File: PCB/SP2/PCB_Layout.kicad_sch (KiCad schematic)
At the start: 5 parts, among them J1 PA1010D, J2 SD Card, J3 BNO055, U1 Pico

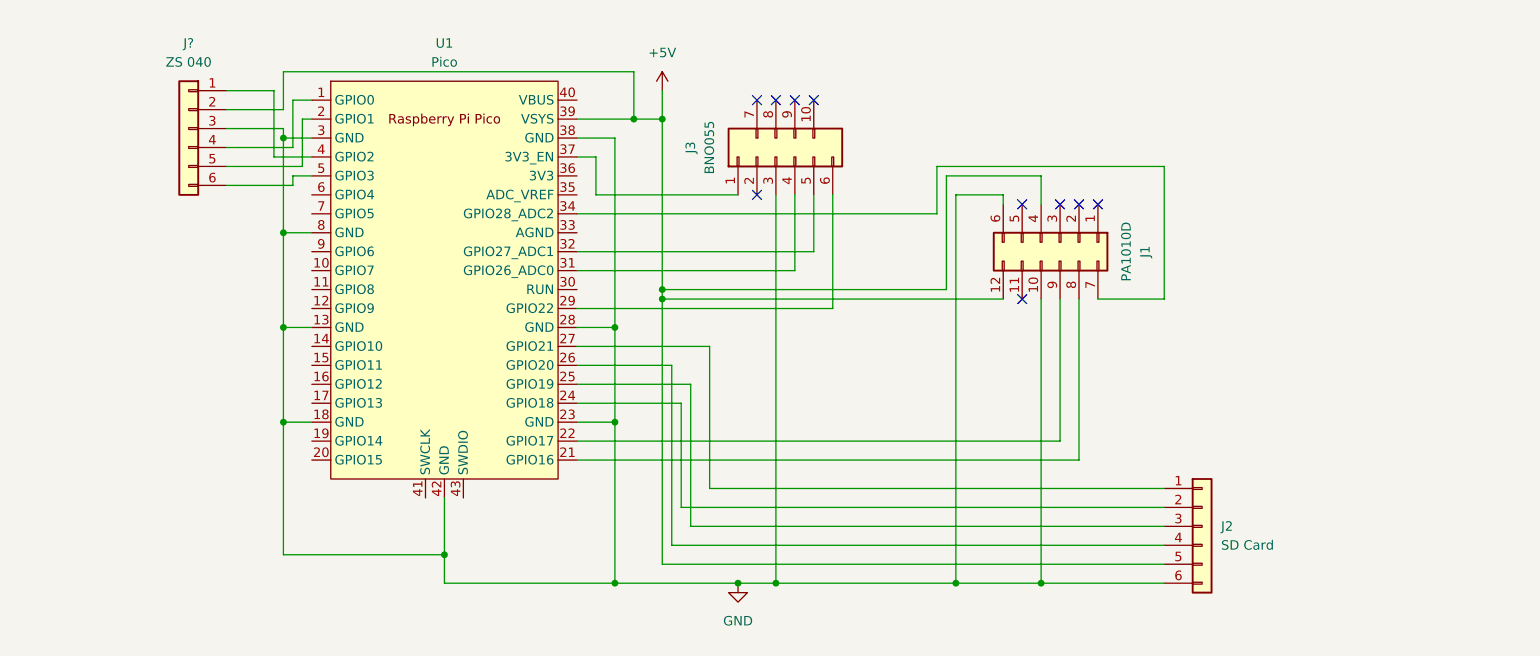
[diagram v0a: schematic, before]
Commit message: Fixed Wires
Cleaned up and fixed the schematic
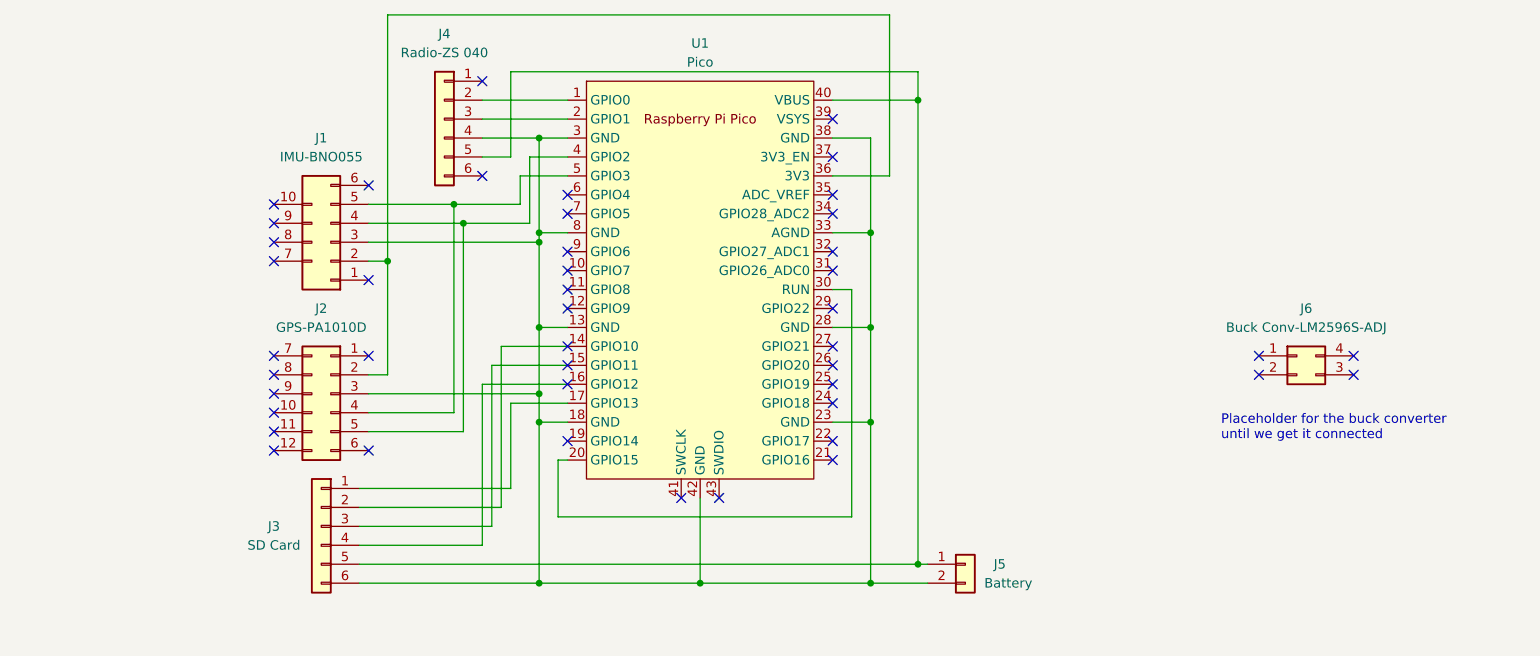
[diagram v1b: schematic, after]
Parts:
- removed J2: SD Card, symbol Connector_Generic:Conn_01x06
- removed J3: BNO055, symbol Connector_Generic:Conn_02x06_Top_Bottom
- added J2: GPS-PA1010D, symbol Connector_Generic:Conn_02x06_Top_Bottom
- added J3: SD Card, symbol Connector_Generic:Conn_01x06
- added J5: Battery, symbol Connector_Generic:Conn_01x02
- added J6: Buck Conv-LM2596S-ADJ, symbol Connector_Generic:Conn_02x02_Counter_Clockwise
- J1: value PA1010D -> IMU-BNO055; footprint (none) -> MCU_RaspberryPi_and_Boards:Adafruit BNO055
- J4: renamed from J?; value ZS 040 -> Radio-ZS 040
- U1: footprint RPi_Pico:RPi_Pico_SMD_TH -> MCU_RaspberryPi_and_Boards:RPi_Pico_SMD_TH
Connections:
- net at J4.4 (Pin_4): now also J1.3 (Pin_3), U1.13 (GND), U1.18 (GND), U1.23 (GND), U1.28 (GND), U1.3 (GND), U1.33 (AGND), U1.38 (GND), U1.42 (GND), U1.8 (GND), J2.3 (Pin_3), J3.6 (Pin_6), J5.2 (Pin_2); no longer U1.1 (GPIO0)
- net at U1.14 (GPIO10): now also J3.2 (Pin_2)
- net at U1.15 (GPIO11): now also J3.3 (Pin_3)
- net at U1.16 (GPIO12): now also J3.4 (Pin_4)
- net at U1.17 (GPIO13): now also J3.1 (Pin_1)
- net at J4.5 (Pin_5): now also U1.40 (VBUS), J3.5 (Pin_5), J5.1 (Pin_1); no longer U1.2 (GPIO1)
- net at U1.20 (GPIO15): now also U1.30 (RUN)
- net at U1.21 (GPIO16): no longer J1.8 (Pin_8)
- net at U1.22 (GPIO17): no longer J1.9 (Pin_9)
- net at U1.34 (GPIO28_ADC2): no longer J1.7 (Pin_7)
- net at U1.36 (3V3): now also J1.2 (Pin_2), J2.2 (Pin_2)
- net at U1.4 (GPIO2): now also J1.4 (Pin_4), J2.5 (Pin_5); no longer J4.1 (Pin_1)
- net at U1.5 (GPIO3): now also J1.5 (Pin_5), J2.4 (Pin_4); no longer J4.6 (Pin_6)
- removed net +5V: J1.12 (Pin_12), J1.4 (Pin_4), J4.2 (Pin_2), U1.39 (VSYS)
- removed net GND: J1.10 (Pin_10), J1.6 (Pin_6), J4.3 (Pin_3), U1.13 (GND), U1.18 (GND), U1.23 (GND), U1.28 (GND), U1.3 (GND), U1.38 (GND), U1.42 (GND), U1.8 (GND)
- new net: J4.2 (Pin_2), U1.1 (GPIO0)
- new net: J4.3 (Pin_3), U1.2 (GPIO1)
- no-connect marks 10 -> 45
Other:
- note added: "Placeholder for the buck converter until we get it connected"
- moved on the sheet: J4, U1

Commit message: Updated PCB and Production files
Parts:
- removed J1: IMU-BNO055, MCU_RaspberryPi_and_Boards:Adafruit BNO055, symbol Connector_Generic:Conn_02x06_Top_Bottom
- removed J2: GPS-PA1010D, symbol Connector_Generic:Conn_02x06_Top_Bottom
- removed J3: SD Card, symbol Connector_Generic:Conn_01x06
- removed J4: Radio-ZS 040, symbol Connector_Generic:Conn_01x06
- removed J5: Battery, symbol Connector_Generic:Conn_01x02
- removed J6: Buck Conv-LM2596S-ADJ, symbol Connector_Generic:Conn_02x02_Counter_Clockwise
- removed U1: Pico, MCU_RaspberryPi_and_Boards:RPi_Pico_SMD_TH, symbol MCU_RaspberryPi_and_Boards:Pico
- added GPS1, IMU1, MicroSD1: SSQ-106-03-G-S, RHDR6W64P254_1X6_1575X241X851P, symbol SSQ-106-03-G-S:SSQ-106-03-G-S
- added Radio1: SSQ-106-02-G-S-RA, RHDRRA6W64P254_1X6_1575X851X241P, symbol SSQ-106-02-G-S-RA:SSQ-106-02-G-S-RA
- added U1: DC_DC_small, DC_DC_LM2596_small:DC_DC_LM2596_small, symbol Custom_dc_dc_small:DC_DC_small
- added U2: Pico, MCU_RaspberryPi_and_Boards:RPi_Pico_SMD_TH, symbol MCU_RaspberryPi_and_Boards:Pico
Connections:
- new net: GPS1.2, IMU1.2, U2.36 (3V3)
- new net: GPS1.3, IMU1.3, MicroSD1.6, Radio1.3, U1.4 (-OUT), U2.13 (GND), U2.18 (GND), U2.23 (GND), U2.28 (GND), U2.3 (GND), U2.38 (GND), U2.8 (GND)
- new net: GPS1.5, IMU1.4, U2.4 (GPIO2)
- new net: GPS1.4, IMU1.5, U2.5 (GPIO3)
- new net: MicroSD1.5, Radio1.2, U1.3 (+OUT), U2.40 (VBUS)
- new net: Radio1.4, U2.2 (GPIO1)
- new net: Radio1.5, U2.1 (GPIO0)
- new net: MicroSD1.2, U2.14 (GPIO10)
- new net: MicroSD1.3, U2.15 (GPIO11)
- new net: MicroSD1.4, U2.16 (GPIO12)
- new net: MicroSD1.1, U2.17 (GPIO13)
- no-connect marks 45 -> 0
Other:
- note removed: "Placeholder for the buck converter until we get it connected"
